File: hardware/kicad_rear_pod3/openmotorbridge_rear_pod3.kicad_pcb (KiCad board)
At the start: 4 copper layers, 70 x 48 mm, 20 parts, among them J1 6-Pin_OMM_Female_Socket, J2 LORA_UFL, J3 GNSS_UFL, U1 ESP32-C3-WROOM-02, U2 MAX-M10S_GNSS, U3 SX1262_LoRa_+22dBm, U4 DS2401_1Wire_ID

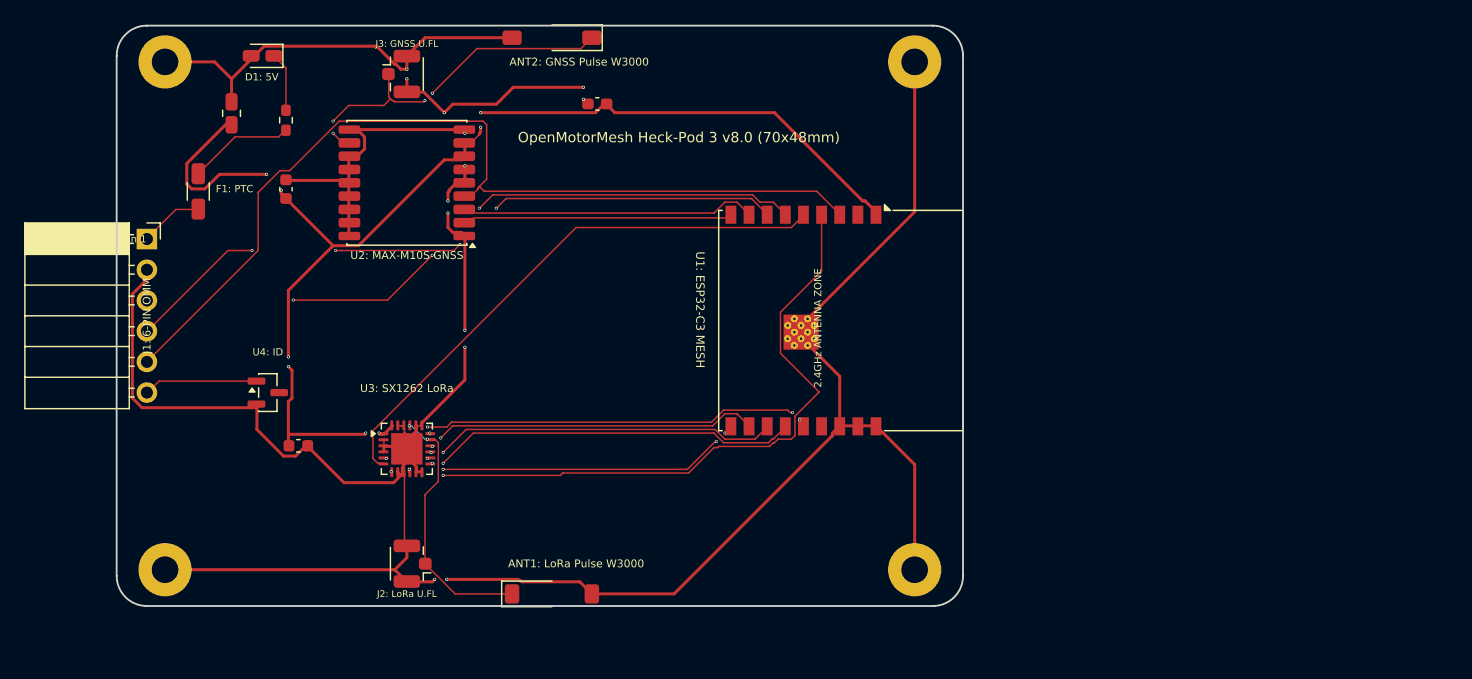
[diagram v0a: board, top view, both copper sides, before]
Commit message: refactor(hardware): remove redundant U.FL connectors on Rear Pod 3 for direct 50 Ohm antenna routing
- Removed J2 (LoRa U.FL) and J3 (GNSS U.FL) SMD connectors to eliminate impedance mismatches, RF reflections, and parasitic open stubs.
- Cleared old U.FL track stubs and unrouted GNSS_RF_IN and LORA_RF_ANT for clean direct 50 Ohm microstrip routing straight from transceivers to Pulse W3000 ceramic antennas.
- Preserved all other 20 fully routed nets (Power, SPI, UART, 1PPS, 1-Wire ID, LEDs).
- Updated generate_rear_pod3_routed_ready.py and refreshed 3D PCB renders.
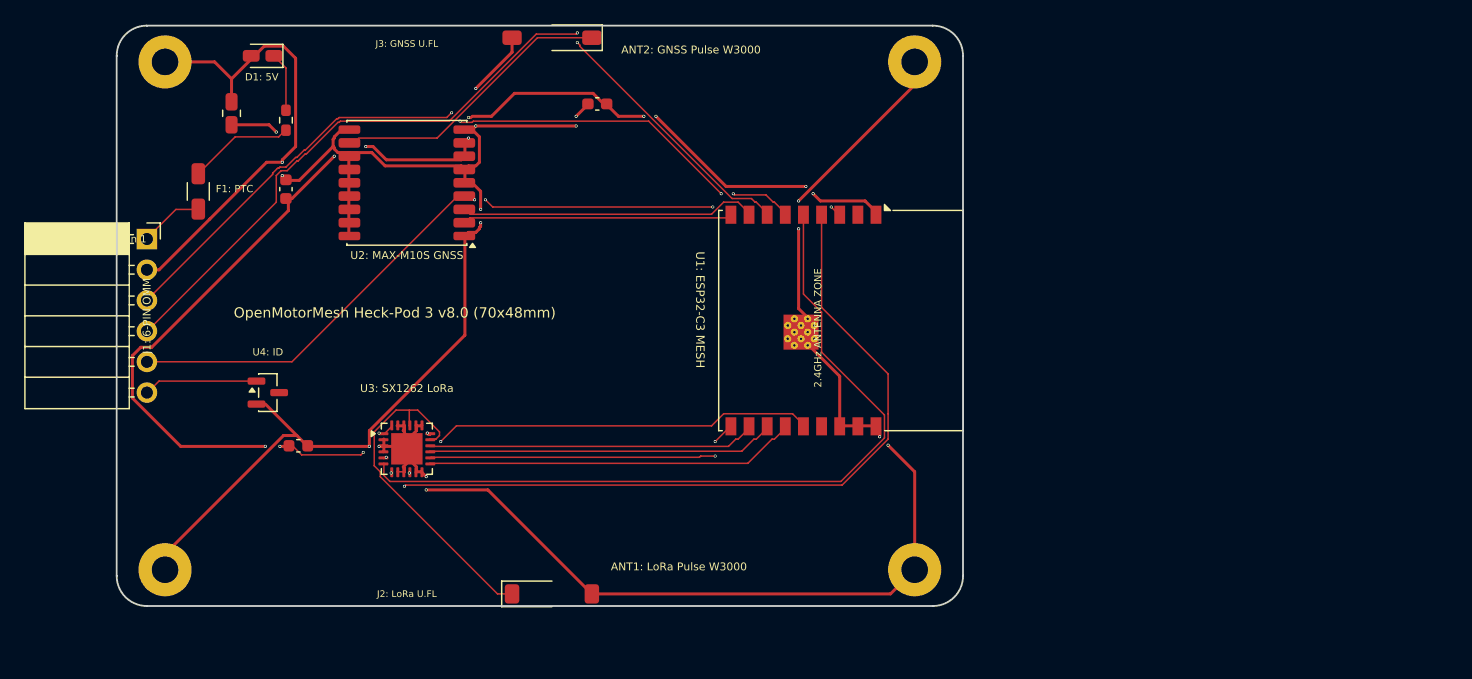
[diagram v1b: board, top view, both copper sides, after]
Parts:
- removed J2: LORA_UFL, Connector_Coaxial.pretty:U.FL_Hirose_U.FL-R-SMT-1_Vertical
- removed J3: GNSS_UFL, Connector_Coaxial.pretty:U.FL_Hirose_U.FL-R-SMT-1_Vertical
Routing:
- net GND: track 282.2 -> 256.1 mm, vias 13 -> 16
- net LORA_BUSY: track 46.5 -> 65.5 mm
- net GNSS_1PPS: track 77.1 -> 62.8 mm, vias 0 -> 4
- net POD3_UART_RX: track 56.4 -> 69.7 mm, vias 4 -> 2
- net VCC_3V3: track 116.3 -> 125.0 mm, vias 10 -> 15
- net LORA_DIO1: track 56.9 -> 64.3 mm
- net LORA_RF_ANT: track 21.8 -> 28.4 mm, vias 2 -> 0
- net GNSS_RF_IN: track 29.3 -> 22.8 mm, vias 4 -> 0
- net POD3_UART_TX: track 57.1 -> 62.9 mm, vias 3 -> 4
- net LORA_NRST: track 41.6 -> 36.8 mm, vias 4 -> 2
- net LORA_MISO: track 29.0 -> 27.3 mm, vias 2 -> 0
- net LORA_MOSI: track 30.7 -> 29.0 mm, vias 2 -> 0
- net LORA_NSS: track 32.4 -> 30.9 mm, vias 2 -> 0
- net LORA_SCK: track 27.7 -> 26.8 mm, vias 4 -> 2
- net GNSS_TXD: track 21.5 -> 22.4 mm

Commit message: feat(hardware): finalize clean re-routing of Rear Pod 3 with direct 50 Ohm antenna paths
- Re-routed openmotorbridge_rear_pod3.kicad_pcb with 100% connectivity and 0 unconnected items.
- Connected u-blox MAX-M10S (GNSS) directly to Pulse W3000 patch antenna without stubs.
- Connected Semtech SX1262 (LoRa) directly to Pulse W3000 ceramic antenna without stubs.
- Verified KiCad DRC: 0 unconnected items.
- Re-rendered 3D top/bottom PCB images.
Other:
- board text removed: "J2: LoRa U.FL"
- board text removed: "J3: GNSS U.FL"

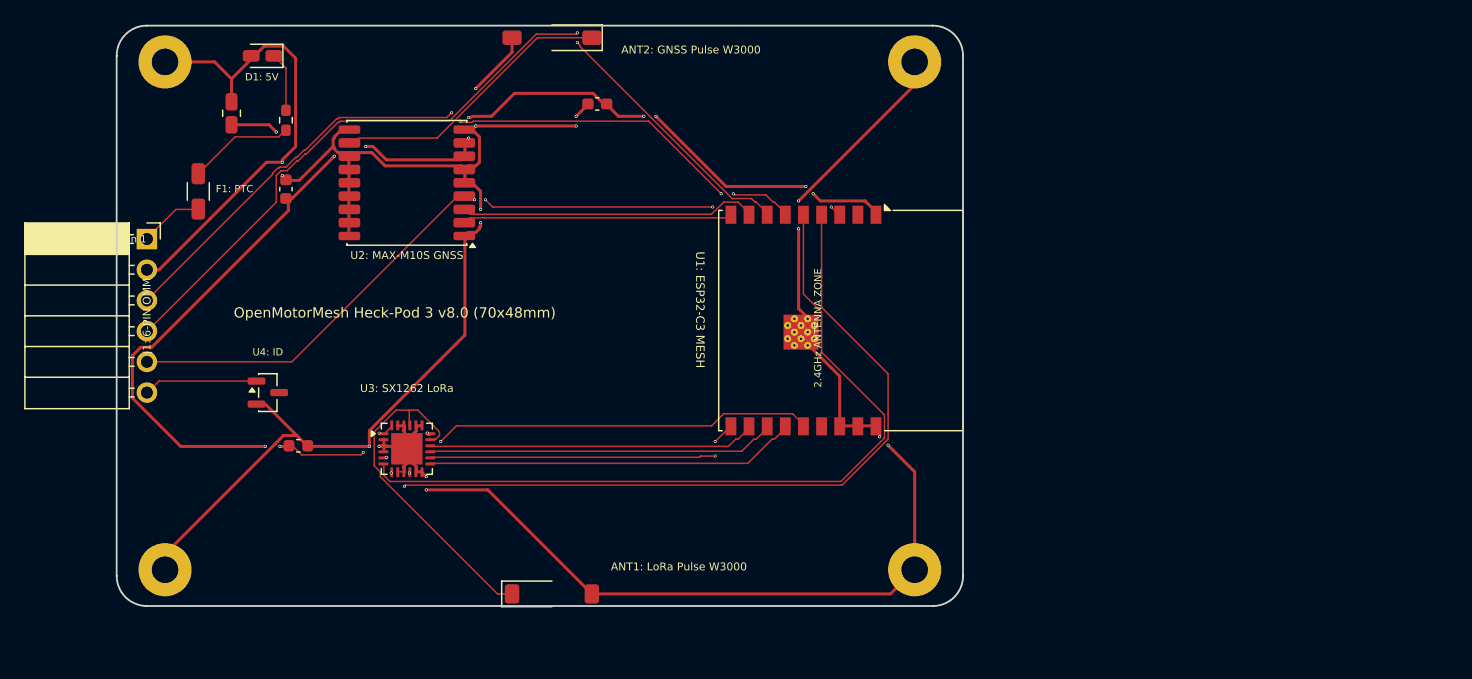
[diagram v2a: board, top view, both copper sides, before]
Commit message: feat(hardware): finalize Pod 3 PCB routing, 110x52mm enclosure, 3x MM8030 RF switches, and manufacturing packages
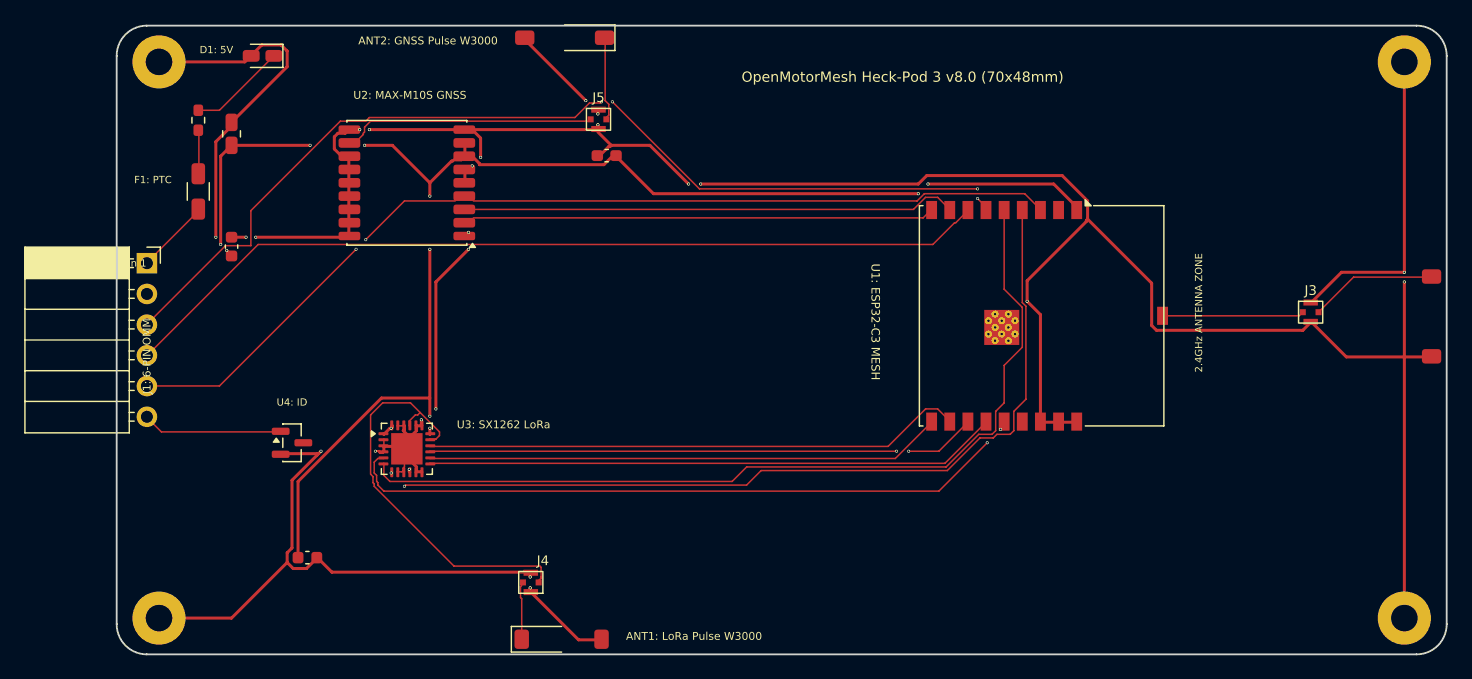
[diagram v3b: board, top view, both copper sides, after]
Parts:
- added ANT3: 2.4GHz_Mesh_Antenna, RF_Antenna.pretty:Pulse_W3000, F.Cu at (208.8, 94.0)
- added J3: MM8030_2G4, RF_Connector.pretty:Murata_MM8030-2610, F.Cu at (198.8, 93.7)
- added J4: MM8030_LORA, RF_Connector.pretty:Murata_MM8030-2610, F.Cu at (134.2, 116.0)
- added J5: MM8030_GNSS, RF_Connector.pretty:Murata_MM8030-2610, F.Cu at (139.8, 77.8)
- moved H4 40.7 mm to (206.5, 119.0)
- moved H2 40.5 mm to (206.5, 73.0)
- moved U1 16.6 mm to (173.4, 94.0)
- moved C4 9.28 mm to (115.8, 114.0)
- moved R1 7.25 mm to (106.8, 77.8)
- moved C3 6.54 mm to (109.5, 88.3)
- moved U4 4.61 mm to (114.5, 104.5)
- moved C2 4.34 mm to (140.5, 80.8)
- moved H3 4.03 mm to (103.5, 119.0)
- moved ANT1 3.83 mm to (136.8, 120.8)
- moved J1 2.00 mm to (102.5, 89.7)
- moved C1 1.70 mm to (109.5, 79.0)
- moved ANT2 1.05 mm to (137.1, 71.0)
- moved H1 0.50 mm to (103.5, 73.0)
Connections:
- ANT1 pad 1: LORA_RF_ANT -> LORA_ANT_INT
- ANT2 pad 1: GNSS_RF_IN -> GNSS_ANT_INT
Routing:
- net GND: track 256.1 -> 359.3 mm, vias 16 -> 23
- net LORA_NRST: track 36.8 -> 57.6 mm
- net POD3_UART_TX: track 62.9 -> 83.0 mm
- net LORA_MISO: track 27.3 -> 44.9 mm
- net GNSS_RXD: track 24.1 -> 41.0 mm
- net GNSS_1PPS: track 62.8 -> 79.6 mm, vias 4 -> 2
- net LORA_NSS: track 30.9 -> 47.5 mm
- net LORA_MOSI: track 29.0 -> 45.6 mm, vias 0 -> 2
- net LORA_SCK: track 26.8 -> 42.9 mm, vias 2 -> 0
- net GNSS_TXD: track 22.4 -> 38.3 mm
- net ESP_RF_ANT: track 0.00 -> 11.7 mm
- net VCC_3V3: track 125.0 -> 136.5 mm, vias 15 -> 12
- net ESP_ANT_INT: track 0.00 -> 10.7 mm
- net LORA_DIO1: track 64.3 -> 73.0 mm
- net LORA_BUSY: track 65.5 -> 73.5 mm
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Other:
- board size 70 x 48 mm -> 110 x 52 mm

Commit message: feat(pcb): resize OMM transceiver board to 55x48mm and pre-place components
- Resized Edge.Cuts to 55.0 x 48.0 mm (R = 2.5 mm)
- Removed obsolete chip antennas (ANT1, ANT2, ANT3) and mechanical switch (J3)
- Replaced J4 (LoRa) and J5 (GNSS) with U.FL footprints
- Replaced U1 with ESP32-C3-WROOM-02U footprint
- Positioned 4x M2 mounting holes matching sled standoffs: H1/H2 at X=103mm, H3/H4 at X=149mm
- Pre-placed components into clean functional zones (Interface, GNSS, LoRa, ESP32)
- Re-rendered photorealistic top and bottom 3D raytraces
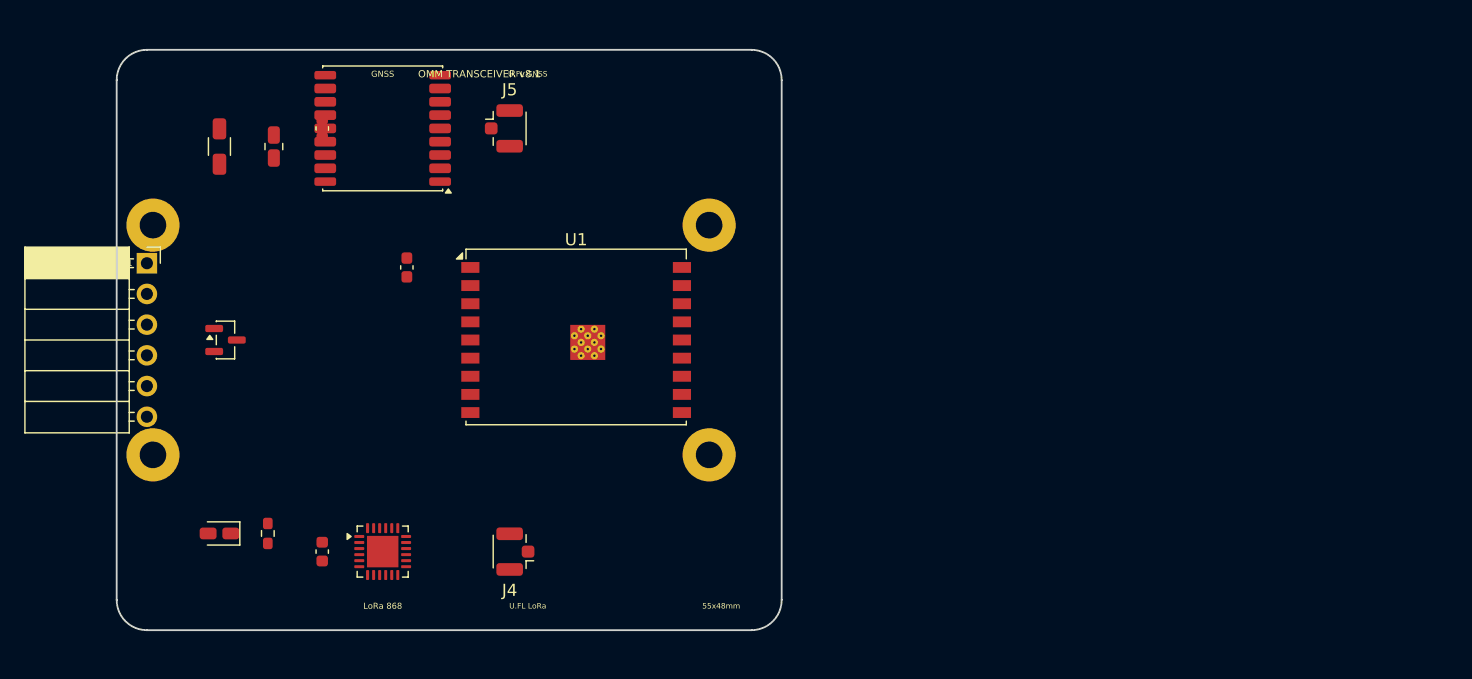
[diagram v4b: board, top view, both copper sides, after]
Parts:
- removed ANT1: 868MHz_LoRa_Antenna, RF_Antenna.pretty:Pulse_W3000
- removed ANT2: GNSS_Patch_Antenna, RF_Antenna.pretty:Pulse_W3000
- removed ANT3: 2.4GHz_Mesh_Antenna, RF_Antenna.pretty:Pulse_W3000
- removed J3: MM8030_2G4, RF_Connector.pretty:Murata_MM8030-2610
- J4: value MM8030_LORA -> U.FL_LORA; footprint RF_Connector.pretty:Murata_MM8030-2610 -> U.FL_Hirose_U.FL-R-SMT-1_Vertical
- J5: value MM8030_GNSS -> U.FL_GNSS; footprint RF_Connector.pretty:Murata_MM8030-2610 -> U.FL_Hirose_U.FL-R-SMT-1_Vertical
- U1: value ESP32-C3-WROOM-02 -> ESP32-C3-WROOM-02U; footprint RF_Module.pretty:ESP32-C3-WROOM-02 -> ESP32-C3-WROOM-02U
- moved H2 108.5 mm to (103.0, 105.5)
- moved H4 59.1 mm to (149.0, 105.5)
- moved H3 55.9 mm to (149.0, 86.5)
- moved D1 39.7 mm to (108.5, 112.0)
- moved U1 35.5 mm to (138.0, 96.0), turned to 0 degrees
- moved R1 34.7 mm to (112.5, 112.0)
- moved C2 18.9 mm to (124.0, 90.0), turned to 90 degrees
- moved H1 13.5 mm to (103.0, 86.5)
- moved C3 12.3 mm to (117.0, 78.5)
- moved U4 10.1 mm to (109.0, 96.0)
- moved U3 8.73 mm to (122.0, 113.5)
- moved J5 7.39 mm to (132.5, 78.5)
- moved U2 4.92 mm to (122.0, 78.5)
- moved F1 4.10 mm to (108.5, 80.0)
- moved C1 3.65 mm to (113.0, 80.0)
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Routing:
- net GND: track 359.3 -> 0.00 mm, vias 23 -> 0
- net VCC_3V3: track 136.5 -> 0.00 mm, vias 12 -> 0
- net POD3_UART_TX: track 83.0 -> 0.00 mm, vias 4 -> 0
- net GNSS_1PPS: track 79.6 -> 0.00 mm, vias 2 -> 0
- net LORA_BUSY: track 73.5 -> 0.00 mm
- net POD3_UART_RX: track 73.0 -> 0.00 mm
- net LORA_DIO1: track 73.0 -> 0.00 mm, vias 2 -> 0
- net LORA_NRST: track 57.6 -> 0.00 mm, vias 2 -> 0
- net LORA_NSS: track 47.5 -> 0.00 mm
- net LORA_MOSI: track 45.6 -> 0.00 mm, vias 2 -> 0
- net LORA_MISO: track 44.9 -> 0.00 mm
- net LORA_SCK: track 42.9 -> 0.00 mm
- net GNSS_RXD: track 41.0 -> 0.00 mm
- net GNSS_TXD: track 38.3 -> 0.00 mm
- net LORA_RF_ANT: track 34.0 -> 0.00 mm
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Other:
- board size 110 x 52 mm -> 55 x 48 mm
- board text added: "55x48mm"
- board text added: "GNSS"
- board text added: "J1"
- board text added: "LoRa 868"
- board text added: "OMM TRANSCEIVER v8.1"
- board text added: "U.FL GNSS"
- board text added: "U.FL LoRa"
- board text removed: "2.4GHz ANTENNA ZONE"
- board text removed: "ANT1: LoRa Pulse W3000"
- board text removed: "ANT2: GNSS Pulse W3000"
- board text removed: "D1: 5V"
- board text removed: "F1: PTC"
- board text removed: "J1: 6-PIN OMM"
- board text removed: "OpenMotorMesh Heck-Pod 3 v8.0 (70x48mm)"
- board text removed: "U1: ESP32-C3 MESH"
- board text removed: "U2: MAX-M10S GNSS"
- board text removed: "U3: SX1262 LoRa"
- board text removed: "U4: ID"
- board text removed: "▲ Pin 1"

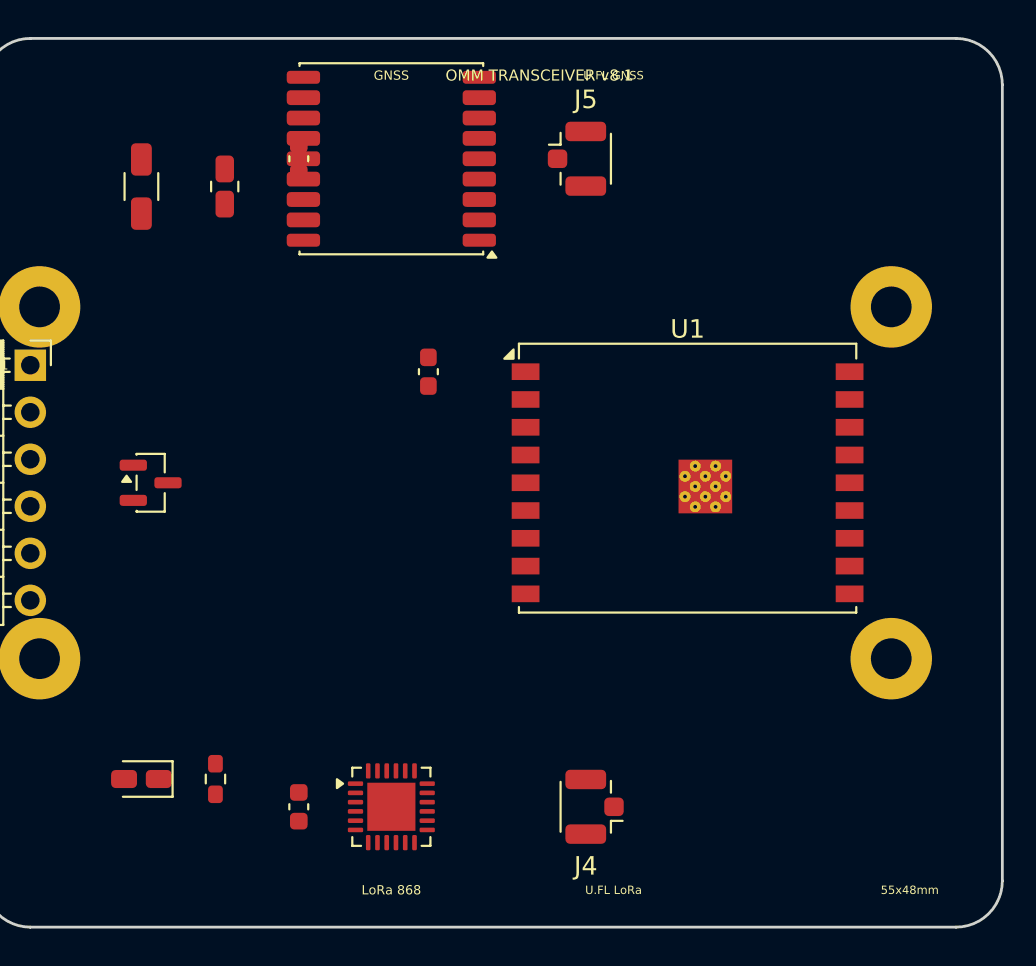
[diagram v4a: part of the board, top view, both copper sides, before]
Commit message: fix(pcb): connect J4 and J5 U.FL shield pads to GND net
- Fixed pin 2 orientation in Connector_Coaxial:U.FL schematic symbol
- Assigned Net GND to both outer shield pads of J4 (LoRa) and J5 (GNSS)
- Regenerated 3D raytrace render
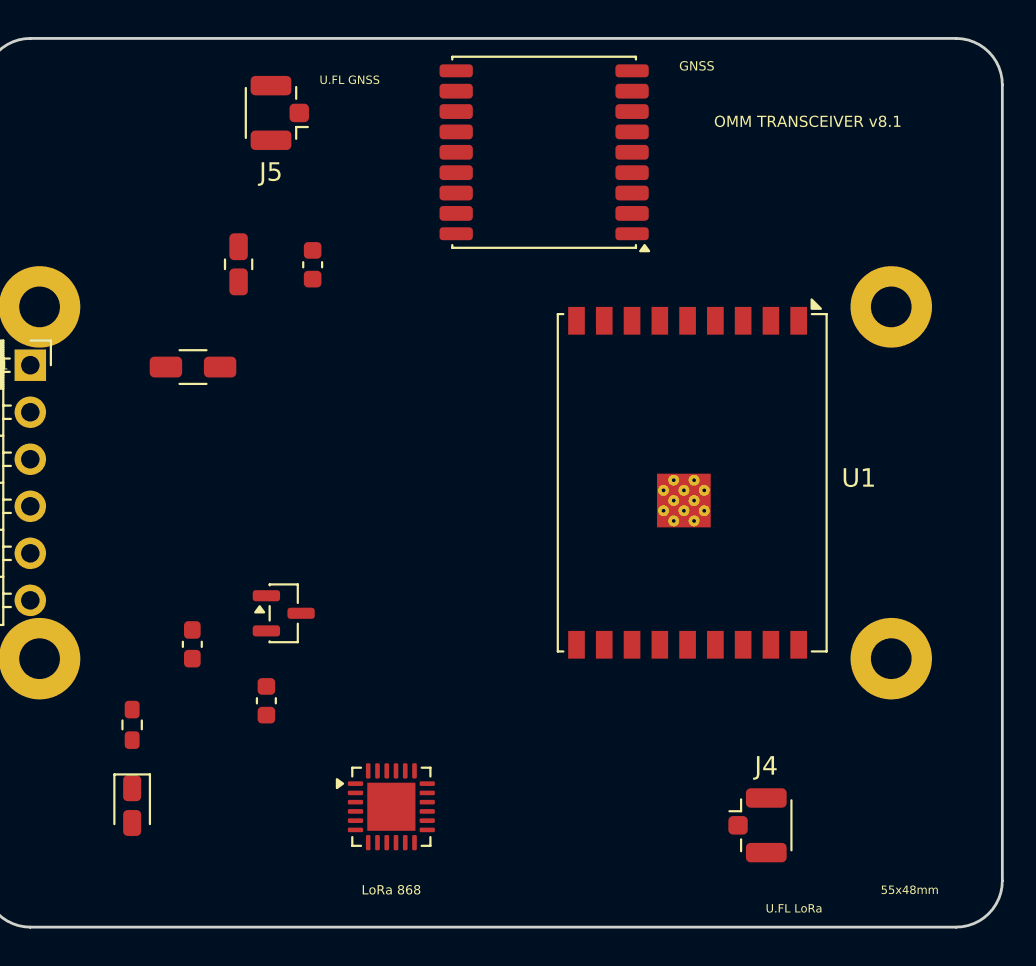
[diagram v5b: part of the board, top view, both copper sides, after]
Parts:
- moved C2 19.5 mm to (111.2, 104.7)
- moved J5 17.2 mm to (115.5, 76.0), turned to 180 degrees
- moved F1 10.1 mm to (111.3, 89.8), turned to 0 degrees
- moved U4 10.1 mm to (116.2, 103.0)
- moved J4 9.80 mm to (142.2, 114.5), turned to 0 degrees
- moved U2 8.26 mm to (130.2, 78.2)
- moved C4 5.99 mm to (115.2, 107.8)
- moved C3 5.77 mm to (117.8, 84.2)
- moved R1 5.37 mm to (108.0, 109.1)
- moved C1 4.27 mm to (113.8, 84.2)
- moved D1 1.52 mm to (108.0, 113.4), turned to -90 degrees
- turned U1 to -90 degrees
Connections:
- J4 pad 2: LORA_ANT_INT -> GND
- J5 pad 2: GNSS_ANT_INT -> GND
